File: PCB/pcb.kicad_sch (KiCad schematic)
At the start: 10 parts

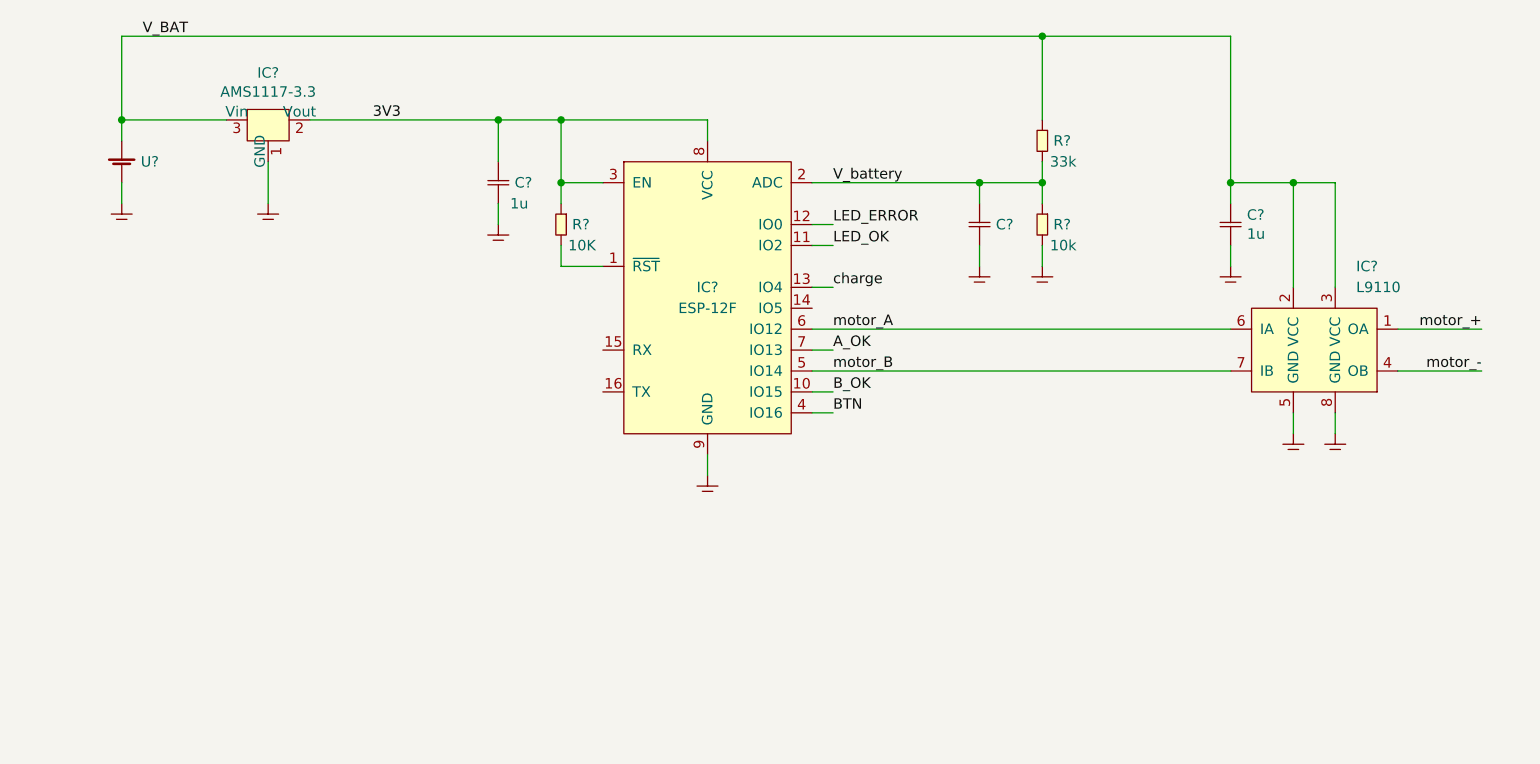
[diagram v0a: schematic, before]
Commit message: added charging circuit, LEDs
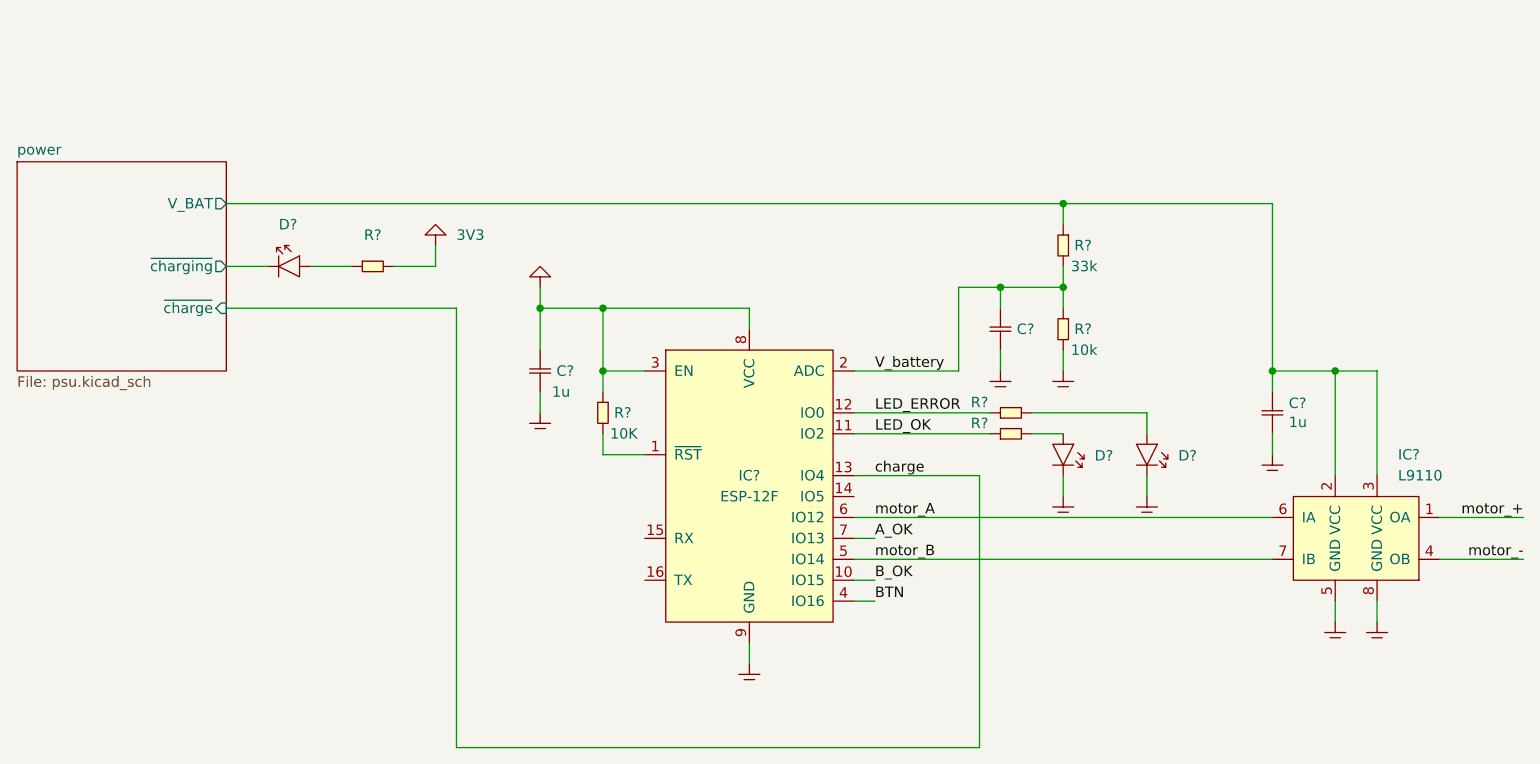
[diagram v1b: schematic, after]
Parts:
- removed C?: C, SMT:0603, symbol pcb-rescue:C-generic
- removed IC?: AMS1117-3.3, SOT:SOT-223, symbol pcb-rescue:AMS1117-3.3-Power
- removed R?: 33k, SMT:0603, symbol pcb-rescue:R-generic
- removed R?: 10k, SMT:0603, symbol pcb-rescue:R-generic
- removed U?: Battery, PCB:battery_wires, symbol pcb-rescue:Battery-generic
- added C?: C, SMT:0603, symbol pcb-rescue:C-generic
- added D? (x3): (no value), symbol generic:LED
- added R? (x3): (no value), symbol generic:R
- added R?: 33k, SMT:0603, symbol pcb-rescue:R-generic
- added R?: 10k, SMT:0603, symbol pcb-rescue:R-generic
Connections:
- net 3V3 is gone; now on net GND: C?.1, IC?.3 (EN), IC?.8 (VCC), R?.1
- net GND: now also C?.2, D?.2 (K), D?.2 (K), R?.2, R?.2
- net LED_ERROR: now also R?.1
- net LED_OK: now also R?.1
- net V_battery: now also C?.1, R?.1, R?.2
- net V_BAT renamed power/V_BAT
- net power/V_BAT: now also R?.1
- new net: D?.1 (A), R?.2 (x2)
- new net: D?.1 (A), R?.1
- new net power/~{charging}: D?.2 (K)
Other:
- added sheet power (psu.kicad_sch)
- moved on the sheet: C?, IC?, R?
